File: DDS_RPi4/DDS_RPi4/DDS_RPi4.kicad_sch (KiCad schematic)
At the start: 34 parts, among them J1 Raspberry_Pi_2_3, J2 Conn_Coaxial, J3 Conn_Coaxial, J4 Conn_01x02_Male, J5 Conn_01x02_Male, T1 Transformer_1P_SS, U1 AD9951, U2 LM1117-1.8, Y2 20M

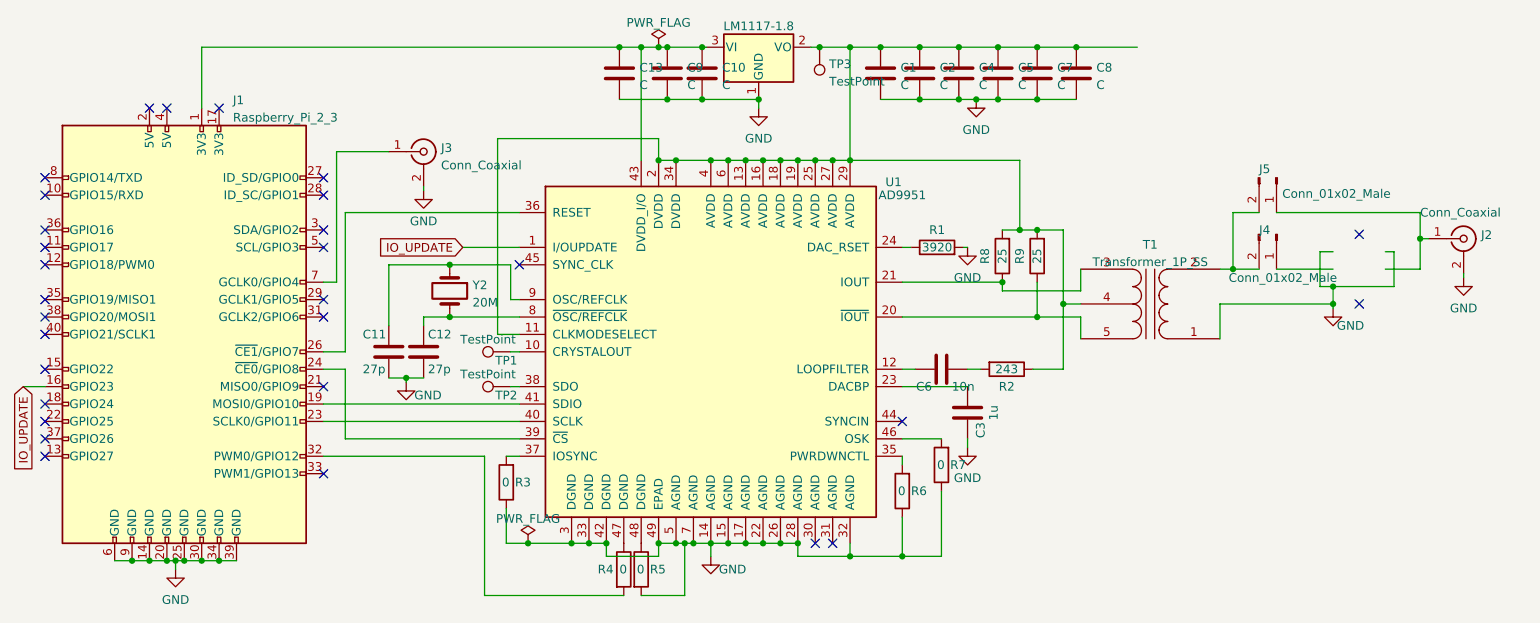
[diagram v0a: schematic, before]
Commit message: update schematic and PCB (disconnect comparator out and add more decoupling capacitors)
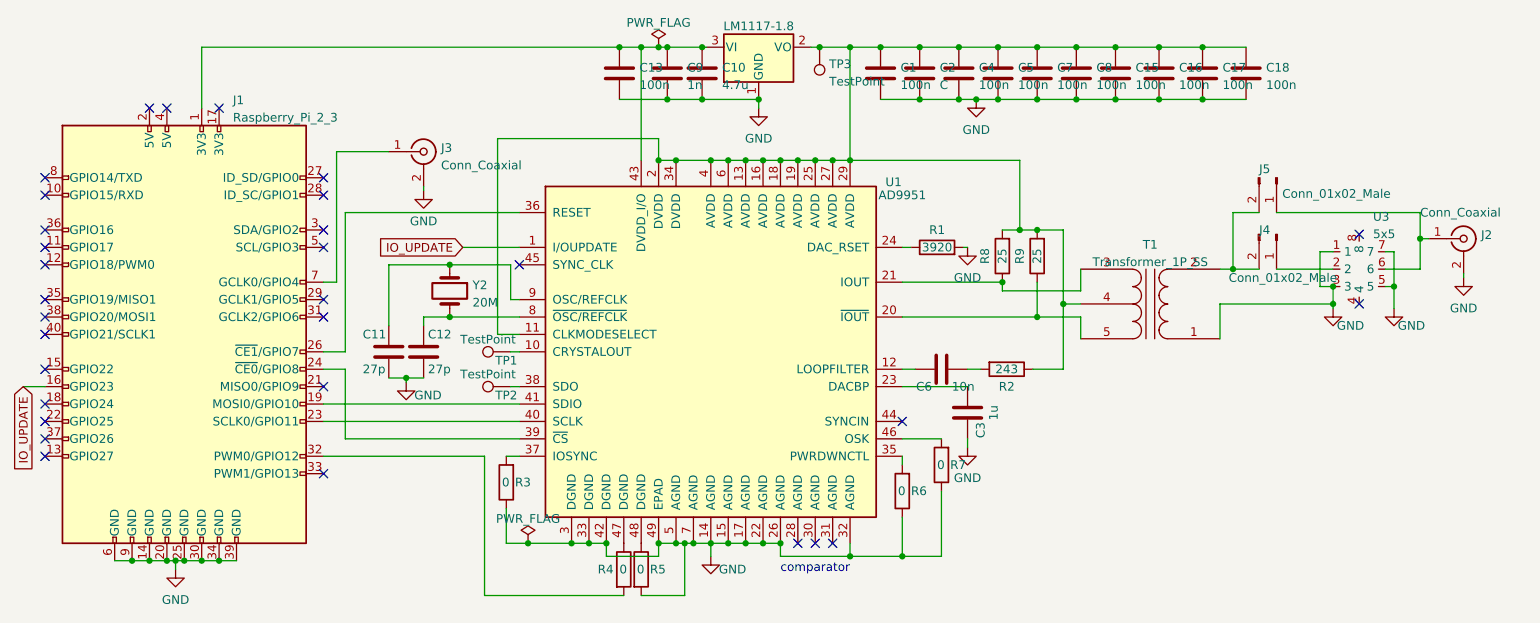
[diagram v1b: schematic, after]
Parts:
- added C15, C16, C17, C18: 100n, Capacitor_SMD:C_0603_1608Metric_Pad1.08x0.95mm_HandSolder, symbol Device:C
- added U3: 5x5, SAW:5x5, symbol SAW:5x5
- C1, C13, C4, C5, C7, C8: value C -> 100n
- C10: value C -> 4.7u
- C9: value C -> 1n
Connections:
- net GND: now also C15.2, C16.2, C17.2, C18.2, U3.1, U3.3, U3.5, U3.7; no longer U1.28 (AGND)
- net at C1.1, C2.1, C4.1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: now also C15.1, C16.1, C17.1, C18.1
- net at J2.1 (In), J5.1 (Pin_1): now also U3.6
- net at J4.1 (Pin_1): now also U3.2
- no-connect marks 30 -> 31
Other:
- note added: "comparator"
